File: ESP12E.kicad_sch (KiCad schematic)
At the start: 58 parts, among them J1 Conn_01x06_Pin, J2 Conn_01x06_Pin, J3 UART, J4 Motor, J5 12v PWR, J6 Sol_1, J7 Sol_2, J8 Sol_3, J9 Sol_4, Q1 IRF520N, Q2 IRF520N, Q3 IRF520N, Q4 IRF520N, Q5 IRF520N, U1 ESP-12E, U2 LM7805_TO220, U3 AMS1117-3.3, U4 HX710(A/B), U5 PSG010R, U6 PSG010R, U7 HX710(A/B)

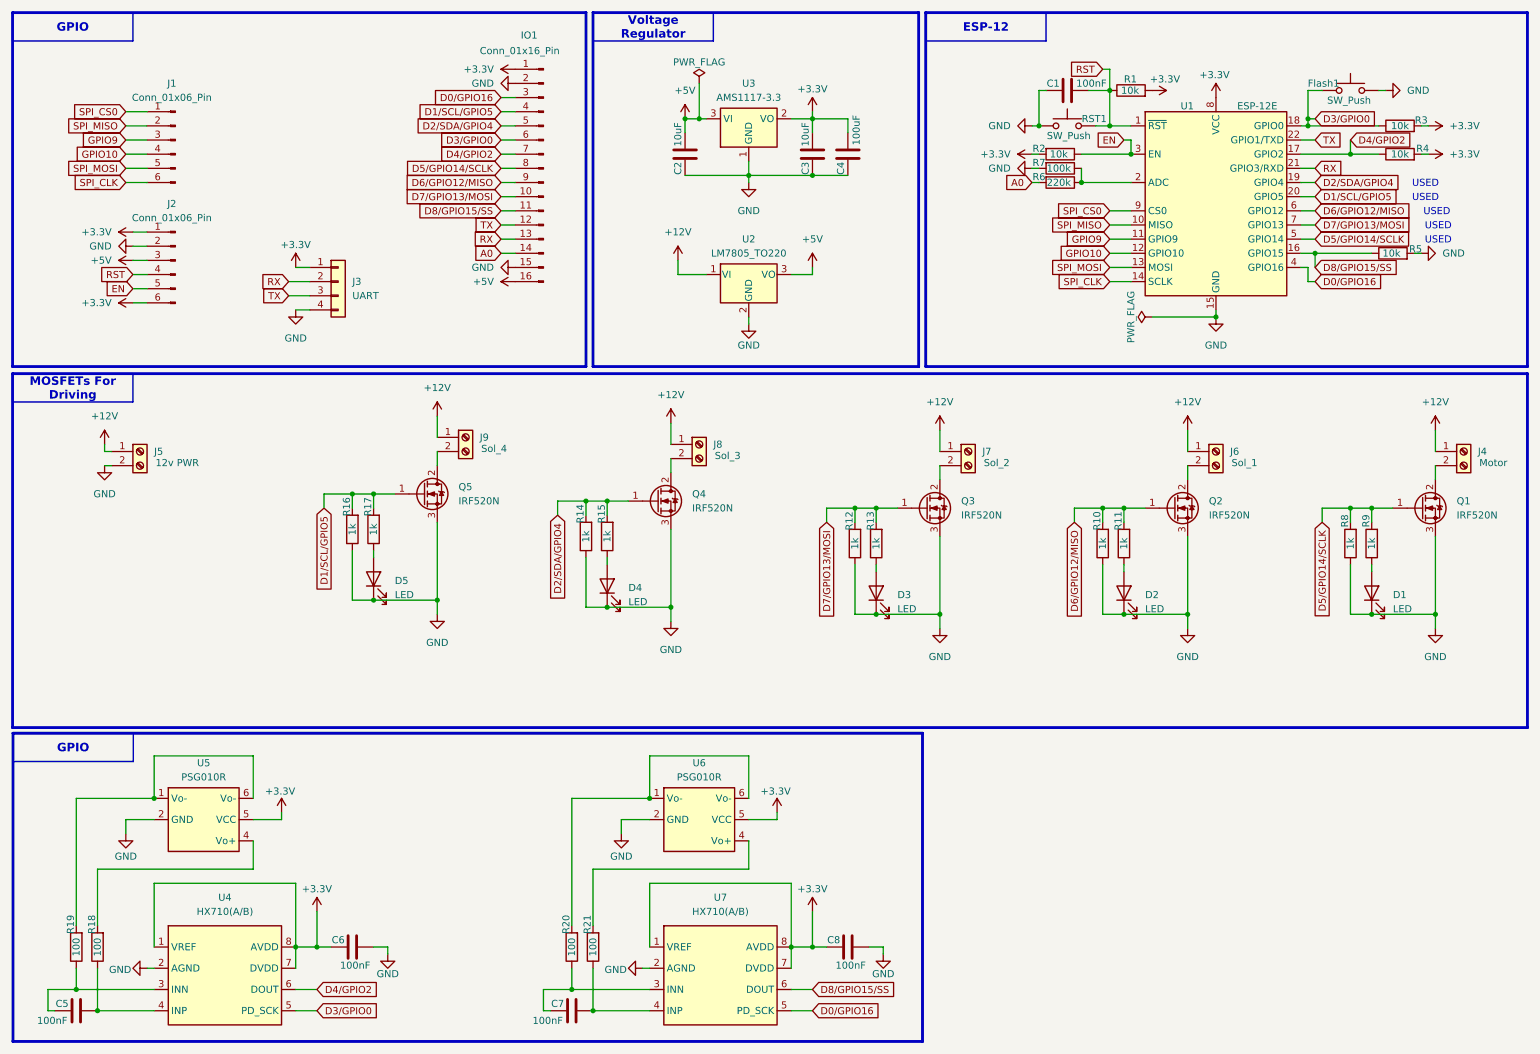
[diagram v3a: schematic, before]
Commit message: feat: the pressure sensor and some protections (flyback diode) is added.
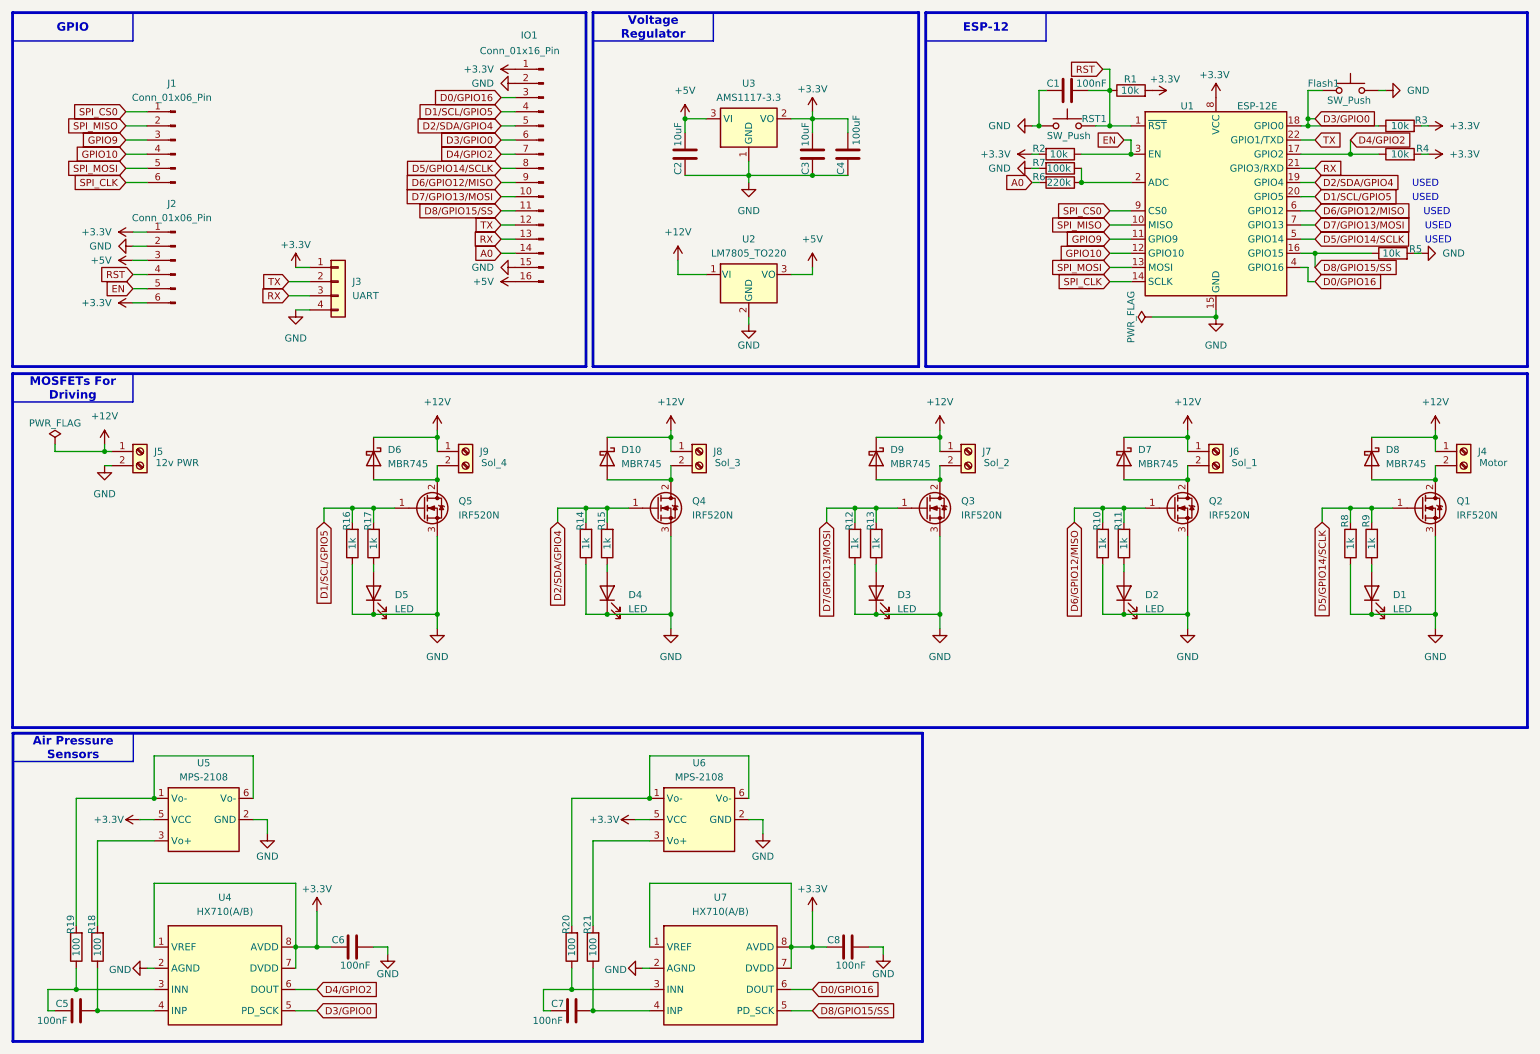
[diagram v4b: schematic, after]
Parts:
- removed U5, U6: PSG010R, Package_DIP:DIP-6_W10.16mm, symbol Sensor_Pressure:PSG010R
- added D10, D6, D7, D8, D9: MBR745, Package_TO_SOT_THT:TO-220-2_Vertical, symbol Diode:MBR745
- added U5, U6: MPS-2108, Package_DIP:DIP-6_W10.16mm, symbol Sensor_Pressure:MPS-2108
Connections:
- net +12V: now also D10.1 (K), D6.1 (K), D7.1 (K), D8.1 (K), D9.1 (K)
- net +3.3V: now also U5.5 (VCC), U6.5 (VCC)
- net D0/GPIO16: now also U7.6 (DOUT); no longer U7.5 (PD_SCK)
- net D8/GPIO15/SS: now also U7.5 (PD_SCK); no longer U7.6 (DOUT)
- net GND: now also U5.2 (GND), U6.2 (GND)
- net RX: now also J3.3 (Pin_3); no longer J3.2 (Pin_2)
- net TX: now also J3.2 (Pin_2); no longer J3.3 (Pin_3)
- net at J7.2 (Pin_2), Q3.2 (D): now also D9.2 (A)
- net at J4.2 (Pin_2), Q1.2 (D): now also D8.2 (A)
- net at R19.2: now also U5.1 (Vo-), U5.6 (Vo-)
- net at J9.2 (Pin_2), Q5.2 (D): now also D6.2 (A)
- net at R20.2: now also U6.1 (Vo-), U6.6 (Vo-)
- net at R21.2: now also U6.3 (Vo+)
- net at R18.2: now also U5.3 (Vo+)
- net at J8.2 (Pin_2), Q4.2 (D): now also D10.2 (A)
- net at J6.2 (Pin_2), Q2.2 (D): now also D7.2 (A)
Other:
- moved on the sheet: D4, D5, J8, J9, Q4, Q5, R14, R15, R16, R17

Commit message: Feat: adding TLP250 for Isolation and driving MOSFETs.
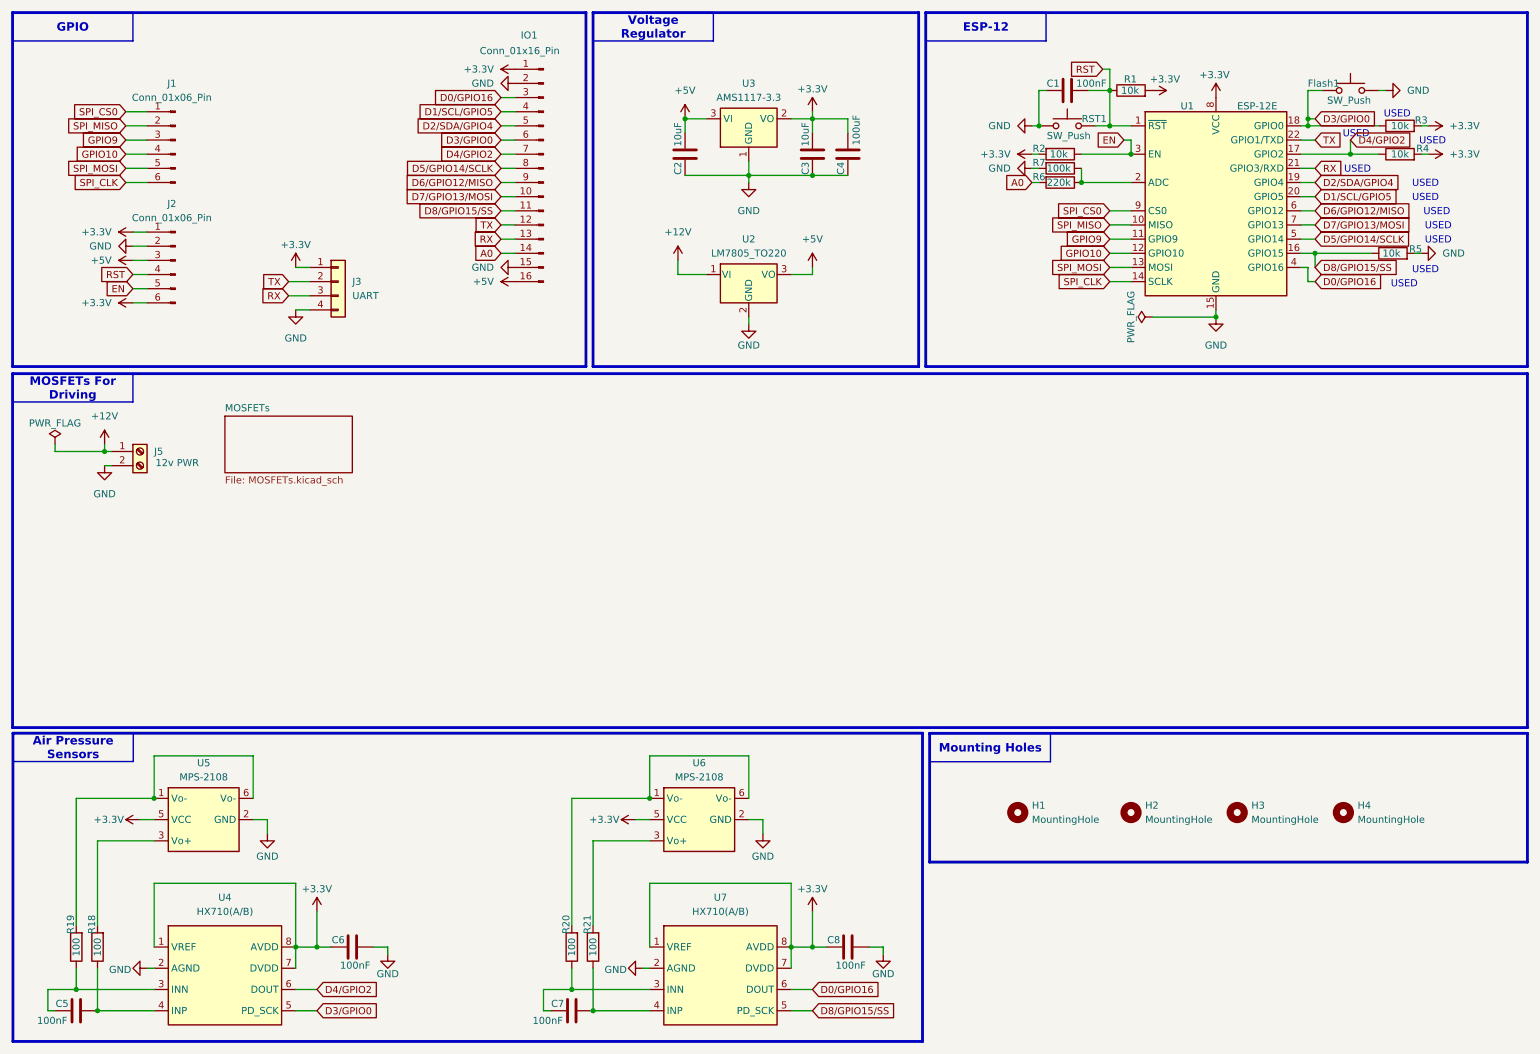
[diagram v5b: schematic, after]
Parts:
- removed D1, D2, D3, D4, D5: LED, LED_SMD:LED_1206_3216Metric, symbol Device:LED
- removed D10, D6, D7, D8, D9: MBR745, Package_TO_SOT_THT:TO-220-2_Vertical, symbol Diode:MBR745
- removed J4: Motor, TerminalBlock_Phoenix:TerminalBlock_Phoenix_PT-1,5-2-5.0-H_1x02_P5.00mm_Horizontal, symbol Connector:Screw_Terminal_01x02
- removed J6: Sol_1, TerminalBlock_Phoenix:TerminalBlock_Phoenix_PT-1,5-2-5.0-H_1x02_P5.00mm_Horizontal, symbol Connector:Screw_Terminal_01x02
- removed J7: Sol_2, TerminalBlock_Phoenix:TerminalBlock_Phoenix_PT-1,5-2-5.0-H_1x02_P5.00mm_Horizontal, symbol Connector:Screw_Terminal_01x02
- removed J8: Sol_3, TerminalBlock_Phoenix:TerminalBlock_Phoenix_PT-1,5-2-5.0-H_1x02_P5.00mm_Horizontal, symbol Connector:Screw_Terminal_01x02
- removed J9: Sol_4, TerminalBlock_Phoenix:TerminalBlock_Phoenix_PT-1,5-2-5.0-H_1x02_P5.00mm_Horizontal, symbol Connector:Screw_Terminal_01x02
- removed Q1, Q2, Q3, Q4, Q5: IRF520N, Package_TO_SOT_THT:TO-220-3_Vertical, symbol Transistor_FET:IRF540N
- removed R10, R11, R12, R13, R14, R15, R16, R17, R8, R9: 1k, Resistor_THT:R_Axial_DIN0309_L9.0mm_D3.2mm_P12.70mm_Horizontal, symbol Device:R
- added H1, H2, H3, H4: MountingHole, MountingHole:MountingHole_2.2mm_M2, symbol Mechanical:MountingHole
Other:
- added sheet MOSFETs (MOSFETs.kicad_sch)

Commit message: working: continue at Work.
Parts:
- J5: footprint TerminalBlock_Phoenix:TerminalBlock_Phoenix_PT-1,5-2-5.0-H_1x02_P5.00mm_Horizontal -> TerminalBlock_RND:TerminalBlock_RND_205-00276_1x02_P5.00mm_Vertical
- R1, R18, R19, R2, R20, R21, R3, R4, R5, R6, R7: footprint Resistor_THT:R_Axial_DIN0309_L9.0mm_D3.2mm_P12.70mm_Horizontal -> Resistor_SMD:R_1206_3216Metric_Pad1.30x1.75mm_HandSolder
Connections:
- net +3.3V: now also J3.3 (Pin_3); no longer J3.1 (Pin_1)
- net RX: now also J3.2 (Pin_2); no longer J3.3 (Pin_3)
- net TX: now also J3.1 (Pin_1); no longer J3.2 (Pin_2)
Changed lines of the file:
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@@
 	(wire
 		(pts
-			(xy 62.23 63.5) (xy 66.04 63.5)
-		)
-		(stroke
-			(width 0)
-			(type default)
-		)
-	)
-	(wire
-		(pts
 			(xy 247.65 26.67) (xy 245.11 26.67)
 		)
@@
 	(wire
 		(pts
+			(xy 55.88 63.5) (xy 66.04 63.5)
+		)
+		(stroke
+			(width 0)
+			(type default)
+		)
+	)
+	(wire
+		(pts
 			(xy 195.58 43.18) (xy 196.85 43.18)
 		)
@@
 	(wire
 		(pts
-			(xy 63.5 58.42) (xy 66.04 58.42)
-		)
-		(stroke
-			(width 0)
-			(type default)
-		)
-	)
-	(wire
-		(pts
 			(xy 27.94 191.77) (xy 27.94 184.15)
 		)
@@
 	(wire
 		(pts
+			(xy 63.5 58.42) (xy 66.04 58.42)
+		)
+		(stroke
+			(width 0)
+			(type default)
+		)
+	)
+	(wire
+		(pts
 			(xy 207.01 33.02) (xy 209.55 33.02)
 		)
@@
 	(wire
 		(pts
+			(xy 55.88 59.69) (xy 55.88 63.5)
+		)
+		(stroke
+			(width 0)
+			(type default)
+		)
+	)
+	(wire
+		(pts
 			(xy 116.84 161.29) (xy 127 161.29)
 		)
@@
 	(wire
 		(pts
-			(xy 62.23 60.96) (xy 66.04 60.96)
+			(xy 63.5 60.96) (xy 66.04 60.96)
 		)
 		(stroke
@@
 	(global_label "RX"
 		(shape input)
-		(at 62.23 63.5 180)
+		(at 63.5 60.96 180)
 		(fields_autoplaced yes)
 		(effects
@@
 		)
 		(property "Intersheetrefs" "${INTERSHEET_REFS}"
-			(at 56.7653 63.5 0)
+			(at 58.0353 60.96 0)
 			(effects
 				(font
@@
 	(global_label "TX"
 		(shape input)
-		(at 62.23 60.96 180)
+		(at 63.5 58.42 180)
 		(fields_autoplaced yes)
 		(effects
@@
 		)
 		(property "Intersheetrefs" "${INTERSHEET_REFS}"
-			(at 57.0677 60.96 0)
+			(at 58.3377 58.42 0)
 			(effects
 				(font
@@
 			)
 		)
-		(property "Footprint" "Resistor_THT:R_Axial_DIN0309_L9.0mm_D3.2mm_P12.70mm_Horizontal"
+		(property "Footprint" "Resistor_SMD:R_1206_3216Metric_Pad1.30x1.75mm_HandSolder"
 			(at 200.66 36.322 90)
 			(effects
@@
 			)
 		)
-		(property "Footprint" "Resistor_THT:R_Axial_DIN0309_L9.0mm_D3.2mm_P12.70mm_Horizontal"
+		(property "Footprint" "Resistor_SMD:R_1206_3216Metric_Pad1.30x1.75mm_HandSolder"
 			(at 261.62 34.798 90)
 			(effects
@@
 			)
 		)
-		(property "Footprint" "Resistor_THT:R_Axial_DIN0309_L9.0mm_D3.2mm_P12.70mm_Horizontal"
+		(property "Footprint" "Resistor_SMD:R_1206_3216Metric_Pad1.30x1.75mm_HandSolder"
 			(at 25.908 180.34 90)
 			(effects
@@
 			)
 		)
-		(property "Footprint" "Resistor_THT:R_Axial_DIN0309_L9.0mm_D3.2mm_P12.70mm_Horizontal"
+		(property "Footprint" "Resistor_SMD:R_1206_3216Metric_Pad1.30x1.75mm_HandSolder"
 			(at 29.718 180.34 90)
 			(effects
@@
 			)
 		)
-		(property "Footprint" "TerminalBlock_Phoenix:TerminalBlock_Phoenix_PT-1,5-2-5.0-H_1x02_P5.00mm_Horizontal"
+		(property "Footprint" "TerminalBlock_RND:TerminalBlock_RND_205-00276_1x02_P5.00mm_Vertical"
 			(at 35.56 91.44 0)
 			(effects
@@
 			)
 		)
-		(property "Footprint" "Resistor_THT:R_Axial_DIN0309_L9.0mm_D3.2mm_P12.70mm_Horizontal"
+		(property "Footprint" "Resistor_SMD:R_1206_3216Metric_Pad1.30x1.75mm_HandSolder"
 			(at 114.808 180.34 90)
 			(effects
@@
 			)
 		)
-		(property "Footprint" "Resistor_THT:R_Axial_DIN0309_L9.0mm_D3.2mm_P12.70mm_Horizontal"
+		(property "Footprint" "Resistor_SMD:R_1206_3216Metric_Pad1.30x1.75mm_HandSolder"
 			(at 118.618 180.34 90)
 			(effects
@@
 			)
 		)
-		(property "Footprint" "Resistor_THT:R_Axial_DIN0309_L9.0mm_D3.2mm_P12.70mm_Horizontal"
+		(property "Footprint" "Resistor_SMD:R_1206_3216Metric_Pad1.30x1.75mm_HandSolder"
 			(at 261.62 39.878 90)
 			(effects
@@
 			)
 		)
-		(property "Footprint" "Resistor_THT:R_Axial_DIN0309_L9.0mm_D3.2mm_P12.70mm_Horizontal"
+		(property "Footprint" "Resistor_SMD:R_1206_3216Metric_Pad1.30x1.75mm_HandSolder"
 			(at 260.35 57.658 90)
 			(effects
@@
 			)
 		)
-		(property "Footprint" "Resistor_THT:R_Axial_DIN0309_L9.0mm_D3.2mm_P12.70mm_Horizontal"
+		(property "Footprint" "Resistor_SMD:R_1206_3216Metric_Pad1.30x1.75mm_HandSolder"
 			(at 213.36 28.448 90)
 			(effects
@@
 			)
 		)
-		(property "Footprint" "Resistor_THT:R_Axial_DIN0309_L9.0mm_D3.2mm_P12.70mm_Horizontal"
+		(property "Footprint" "Resistor_SMD:R_1206_3216Metric_Pad1.30x1.75mm_HandSolder"
 			(at 200.66 38.862 90)
 			(effects
@@
 	(symbol
 		(lib_id "power:+3.3V")
-		(at 63.5 58.42 0)
+		(at 55.88 59.69 0)
 		(unit 1)
 		(exclude_from_sim no)
@@
 		(dnp no)
 		(property "Reference" "#PWR022"
-			(at 63.5 62.23 0)
+			(at 55.88 63.5 0)
 			(effects
 				(font
@@
 		)
 		(property "Value" "+3.3V"
-			(at 63.5 54.356 0)
+			(at 55.88 55.626 0)
 			(effects
 				(font
@@
 		)
 		(property "Footprint" ""
-			(at 63.5 58.42 0)
+			(at 55.88 59.69 0)
 			(effects
 				(font
@@
 		)
 		(property "Datasheet" ""
-			(at 63.5 58.42 0)
+			(at 55.88 59.69 0)
 			(effects
 				(font
@@
 		)
 		(property "Description" "Power symbol creates a global label with name \"+3.3V\""
-			(at 63.5 58.42 0)
+			(at 55.88 59.69 0)
 			(effects
 				(font
@@
 			)
 		)
-		(property "Footprint" "Resistor_THT:R_Axial_DIN0309_L9.0mm_D3.2mm_P12.70mm_Horizontal"
+		(property "Footprint" "Resistor_SMD:R_1206_3216Metric_Pad1.30x1.75mm_HandSolder"
 			(at 200.66 41.402 90)
 			(effects
@@
 	)
 	(sheet
-		(at 50.8 85.09)
+		(at 20.32 113.03)
 		(size 22.86 10.16)
 		(exclude_from_sim no)
@@
 		)
 		(property "Sheetname" "MOSFETs"
-			(at 50.8 84.3784 0)
+			(at 20.32 112.3184 0)
 			(effects
 				(font
@@
 		)
 		(property "Sheetfile" "MOSFETs.kicad_sch"
-			(at 50.8 95.8346 0)
+			(at 20.32 123.7746 0)
 			(effects
 				(font
